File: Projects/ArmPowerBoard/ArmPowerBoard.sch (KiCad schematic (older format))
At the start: 8 parts, among them J1 22V Output, J2 12V Output, P1 BATT_CON, U1 IQL24040A050V-009-R-ND

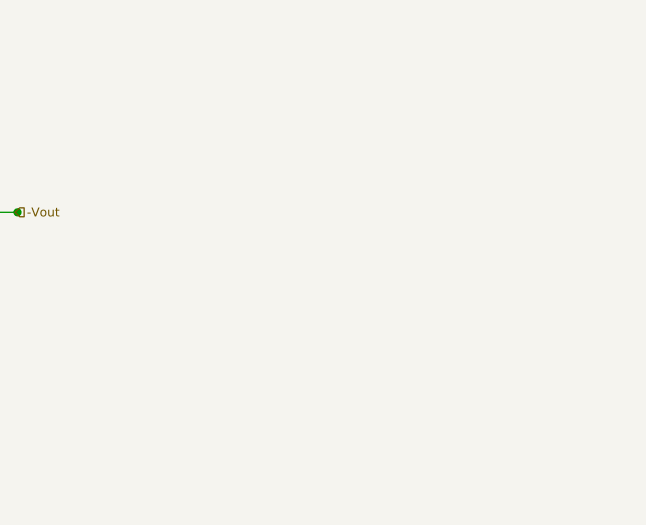
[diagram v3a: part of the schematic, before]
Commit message: adding usb3.0 on arm power board
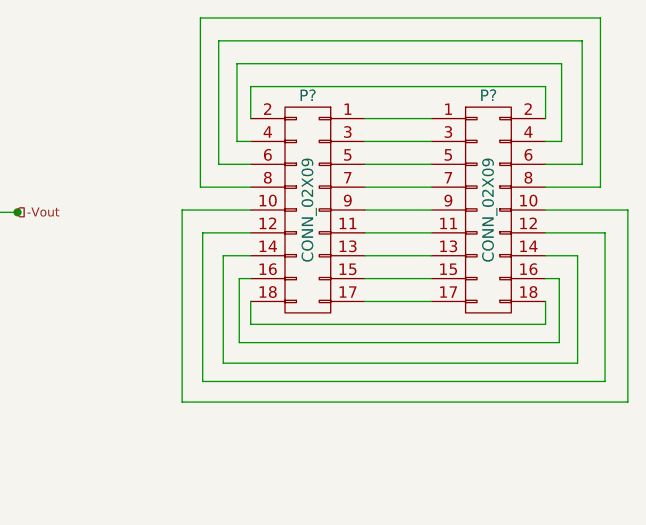
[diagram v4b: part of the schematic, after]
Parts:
- added P? (x2): CONN_02X09, symbol CONN_02X09
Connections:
- new net: P?.1 (P1), P?.1 (P1)
- new net: P?.10 (P10), P?.10 (P10)
- new net: P?.11 (P11), P?.11 (P11)
- new net: P?.12 (P12), P?.12 (P12)
- new net: P?.13 (P13), P?.13 (P13)
- new net: P?.14 (P14), P?.14 (P14)
- new net: P?.15 (P15), P?.15 (P15)
- new net: P?.16 (P16), P?.16 (P16)
- new net: P?.17 (P17), P?.17 (P17)
- new net: P?.18 (P18), P?.18 (P18)
- new net: P?.2 (P2), P?.2 (P2)
- new net: P?.3 (P3), P?.3 (P3)
- new net: P?.4 (P4), P?.4 (P4)
- new net: P?.5 (P5), P?.5 (P5)
- new net: P?.6 (P6), P?.6 (P6)
- new net: P?.7 (P7), P?.7 (P7)
- new net: P?.8 (P8), P?.8 (P8)
- new net: P?.9 (P9), P?.9 (P9)
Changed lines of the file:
@@
 LIBS:contrib
 LIBS:valves
+LIBS:USST-parts
 LIBS:ArmPowerBoard-cache
 EELAYER 25 0
@@
 Connection ~ 3420 3270
 Connection ~ 6190 2820
+$Comp
+L CONN_02X09 P?
+U 1 1 5AE39209
+P 9700 2620
+F 0 "P?" H 9700 3120 50  0000 C CNN
+F 1 "CONN_02X09" V 9700 2620 50  0000 C CNN
+F 2 "" H 9700 1420 50  0000 C CNN
+F 3 "" H 9700 1420 50  0000 C CNN
+	1    9700 2620
+	1    0    0    -1
+$EndComp
+$Comp
+L CONN_02X09 P?
+U 1 1 5AE39247
+P 8910 2620
+F 0 "P?" H 8910 3120 50  0000 C CNN
+F 1 "CONN_02X09" V 8910 2620 50  0000 C CNN
+F 2 "" H 8910 1420 50  0000 C CNN
+F 3 "" H 8910 1420 50  0000 C CNN
+	1    8910 2620
+	-1   0    0    -1
+$EndComp
+Wire Wire Line
+	9160 2220 9450 2220
+Wire Wire Line
+	9160 2320 9450 2320
+Wire Wire Line
+	9160 2420 9450 2420
+Wire Wire Line
+	9160 2520 9450 2520
+Wire Wire Line
+	9160 2620 9450 2620
+Wire Wire Line
+	9160 2720 9450 2720
+Wire Wire Line
+	9160 2820 9450 2820
+Wire Wire Line
+	9160 2920 9450 2920
+Wire Wire Line
+	9160 3020 9450 3020
+Wire Wire Line
+	8660 2220 8660 2080
+Wire Wire Line
+	8660 2080 9950 2080
+Wire Wire Line
+	9950 2080 9950 2220
+Wire Wire Line
+	8660 3020 8660 3120
+Wire Wire Line
+	8660 3120 9950 3120
+Wire Wire Line
+	9950 3120 9950 3020
+Wire Wire Line
+	8660 2920 8610 2920
+Wire Wire Line
+	8610 2920 8610 3200
+Wire Wire Line
+	8610 3200 10010 3200
+Wire Wire Line
+	10010 3200 10010 2920
+Wire Wire Line
+	10010 2920 9950 2920
+Wire Wire Line
+	8660 2320 8600 2320
+Wire Wire Line
+	8600 2320 8600 1980
+Wire Wire Line
+	8600 1980 10020 1980
+Wire Wire Line
+	10020 1980 10020 2320
+Wire Wire Line
+	10020 2320 9950 2320
+Wire Wire Line
+	8660 2420 8520 2420
+Wire Wire Line
+	8520 2420 8520 1880
+Wire Wire Line
+	8520 1880 10110 1880
+Wire Wire Line
+	10110 1880 10110 2420
+Wire Wire Line
+	10110 2420 9950 2420
+Wire Wire Line
+	8660 2820 8540 2820
+Wire Wire Line
+	8540 2820 8540 3290
+Wire Wire Line
+	8540 3290 10090 3290
+Wire Wire Line
+	10090 3290 10090 2820
+Wire Wire Line
+	10090 2820 9950 2820
+Wire Wire Line
+	8660 2520 8440 2520
+Wire Wire Line
+	8440 2520 8440 1780
+Wire Wire Line
+	8440 1780 10190 1780
+Wire Wire Line
+	10190 1780 10190 2520
+Wire Wire Line
+	10190 2520 9950 2520
+Wire Wire Line
+	8660 2720 8450 2720
+Wire Wire Line
+	8450 2720 8450 3370
+Wire Wire Line
+	8450 3370 10210 3370
+Wire Wire Line
+	10210 3370 10210 2720
+Wire Wire Line
+	10210 2720 9950 2720
+Wire Wire Line
+	8660 2620 8360 2620
+Wire Wire Line
+	8360 2620 8360 3460
+Wire Wire Line
+	8360 3460 10310 3460
+Wire Wire Line
+	10310 3460 10310 2620
+Wire Wire Line
+	10310 2620 9950 2620
 $EndSCHEMATC

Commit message: Simple update to APB, also updated its BoM
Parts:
- gave numbers to parts that had none: 2
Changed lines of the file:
@@
 Connection ~ 6190 2820
 $Comp
-L CONN_02X09 P?
+L CONN_02X09 P3
 U 1 1 5AE39209
 P 9700 2620
-F 0 "P?" H 9700 3120 50  0000 C CNN
+F 0 "P3" H 9700 3120 50  0000 C CNN
 F 1 "CONN_02X09" V 9700 2620 50  0000 C CNN
 F 2 "" H 9700 1420 50  0000 C CNN
@@
 $EndComp
 $Comp
-L CONN_02X09 P?
+L CONN_02X09 P2
 U 1 1 5AE39247
 P 8910 2620
-F 0 "P?" H 8910 3120 50  0000 C CNN
+F 0 "P2" H 8910 3120 50  0000 C CNN
 F 1 "CONN_02X09" V 8910 2620 50  0000 C CNN
 F 2 "" H 8910 1420 50  0000 C CNN
